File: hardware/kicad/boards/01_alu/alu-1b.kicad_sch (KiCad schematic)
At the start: 4 parts, among them U301 74HC86, U302 74LS08

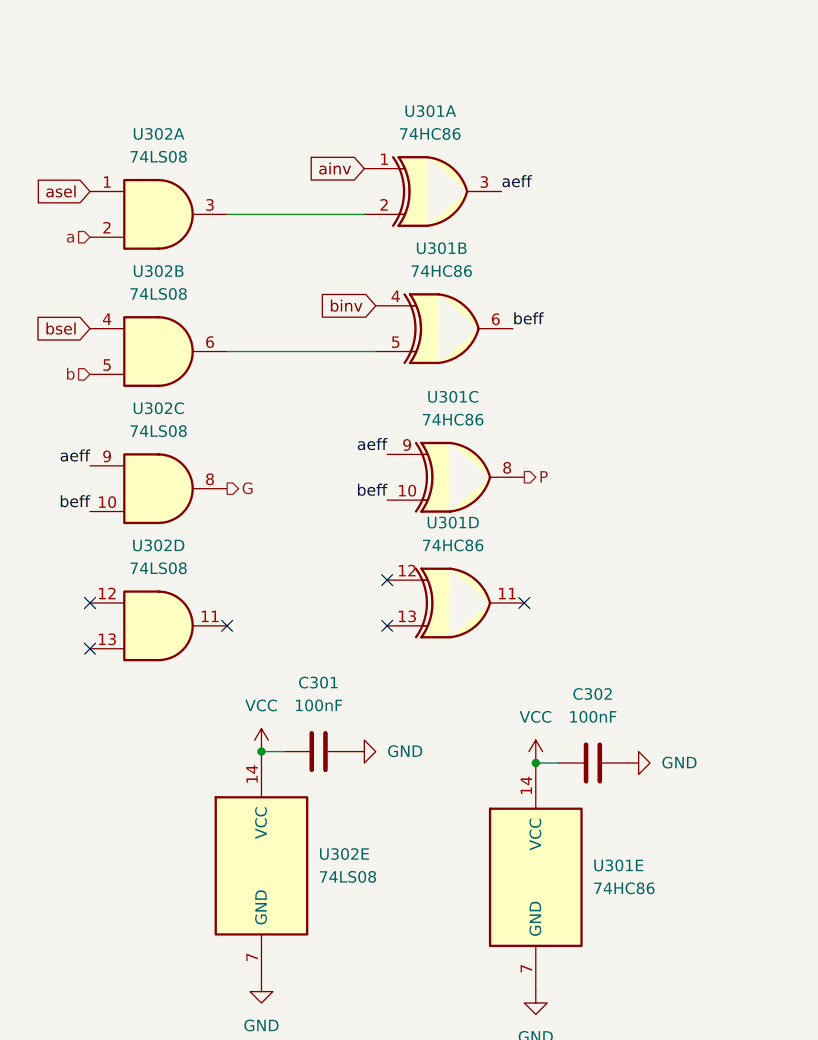
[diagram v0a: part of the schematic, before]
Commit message: arch: added LEDs, override switches; fixed errors and warnings to 0
ready for routing after logical coherence check
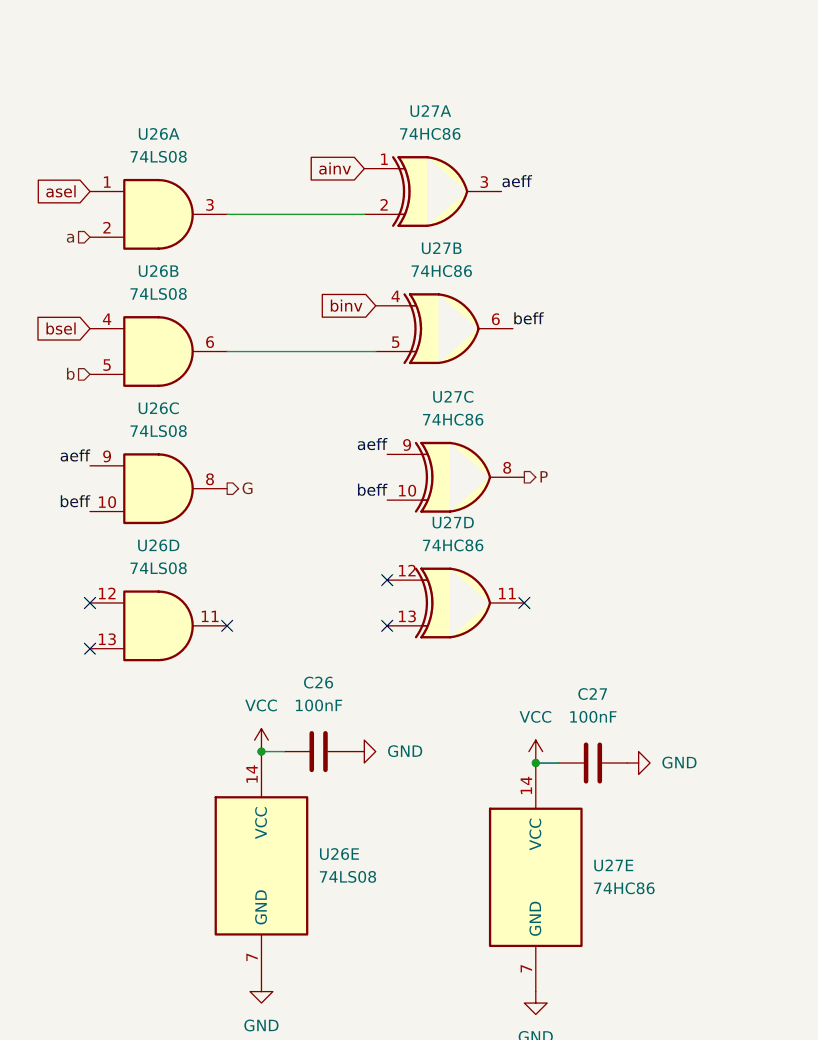
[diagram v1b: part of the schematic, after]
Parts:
- removed U302: 74LS08, Package_SO:SOIC-14_3.9x8.7mm_P1.27mm, symbol 74xx:74LS08
- added U26: 74LS08, Package_SO:SOIC-14_3.9x8.7mm_P1.27mm, symbol 74xx:74LS08
- renumbered C301 to C26, C302 to C27, U301 to U27
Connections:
- net G: now also U26.8
- net GND: now also U26.7 (GND)
- net VCC: now also U26.14 (VCC)
- net a: now also U26.2
- net aeff: now also U26.9
- net asel: now also U26.1
- net b: now also U26.5
- net beff: now also U26.10
- net bsel: now also U26.4
- net at U27.2: now also U26.3
- net at U27.5: now also U26.6

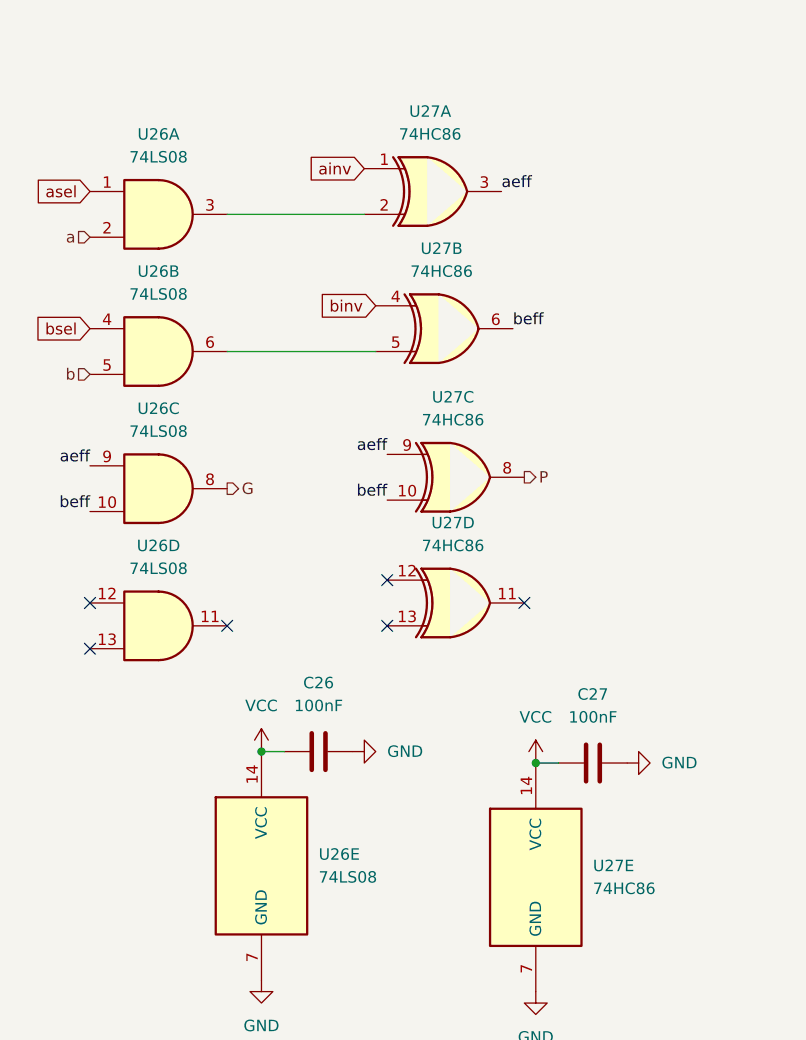
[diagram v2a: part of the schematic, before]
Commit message: design: designed and locked in pcb dimension and component placements
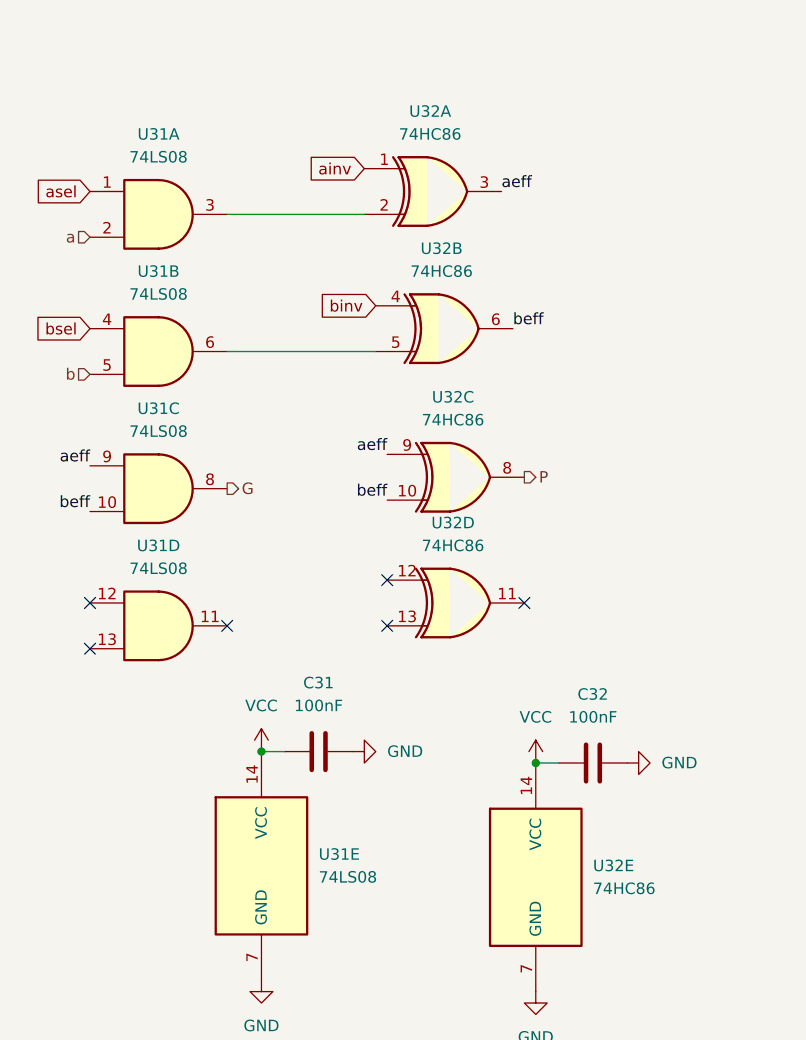
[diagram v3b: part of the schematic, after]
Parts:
- renumbered C26 to C31, C27 to C32, U26 to U31, U27 to U32

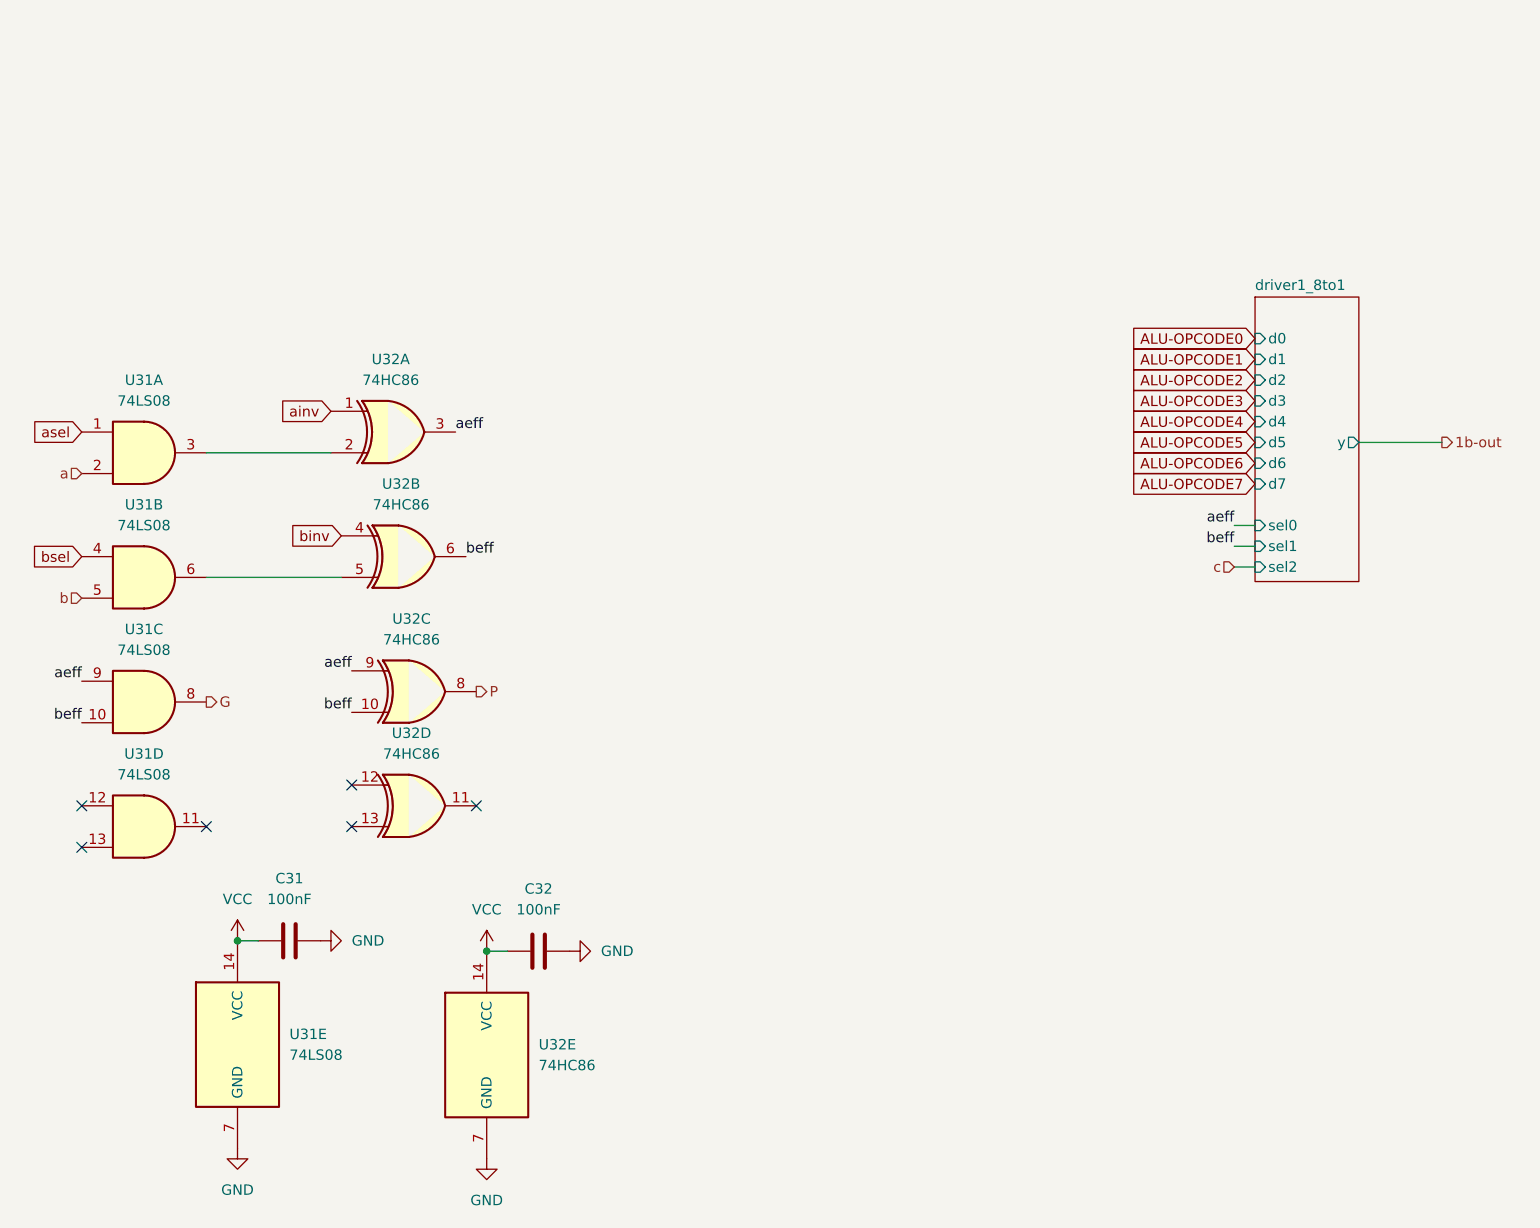
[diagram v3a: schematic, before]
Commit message: arch: replaced 3 footpring 125+138 with one strong 8to1 mux
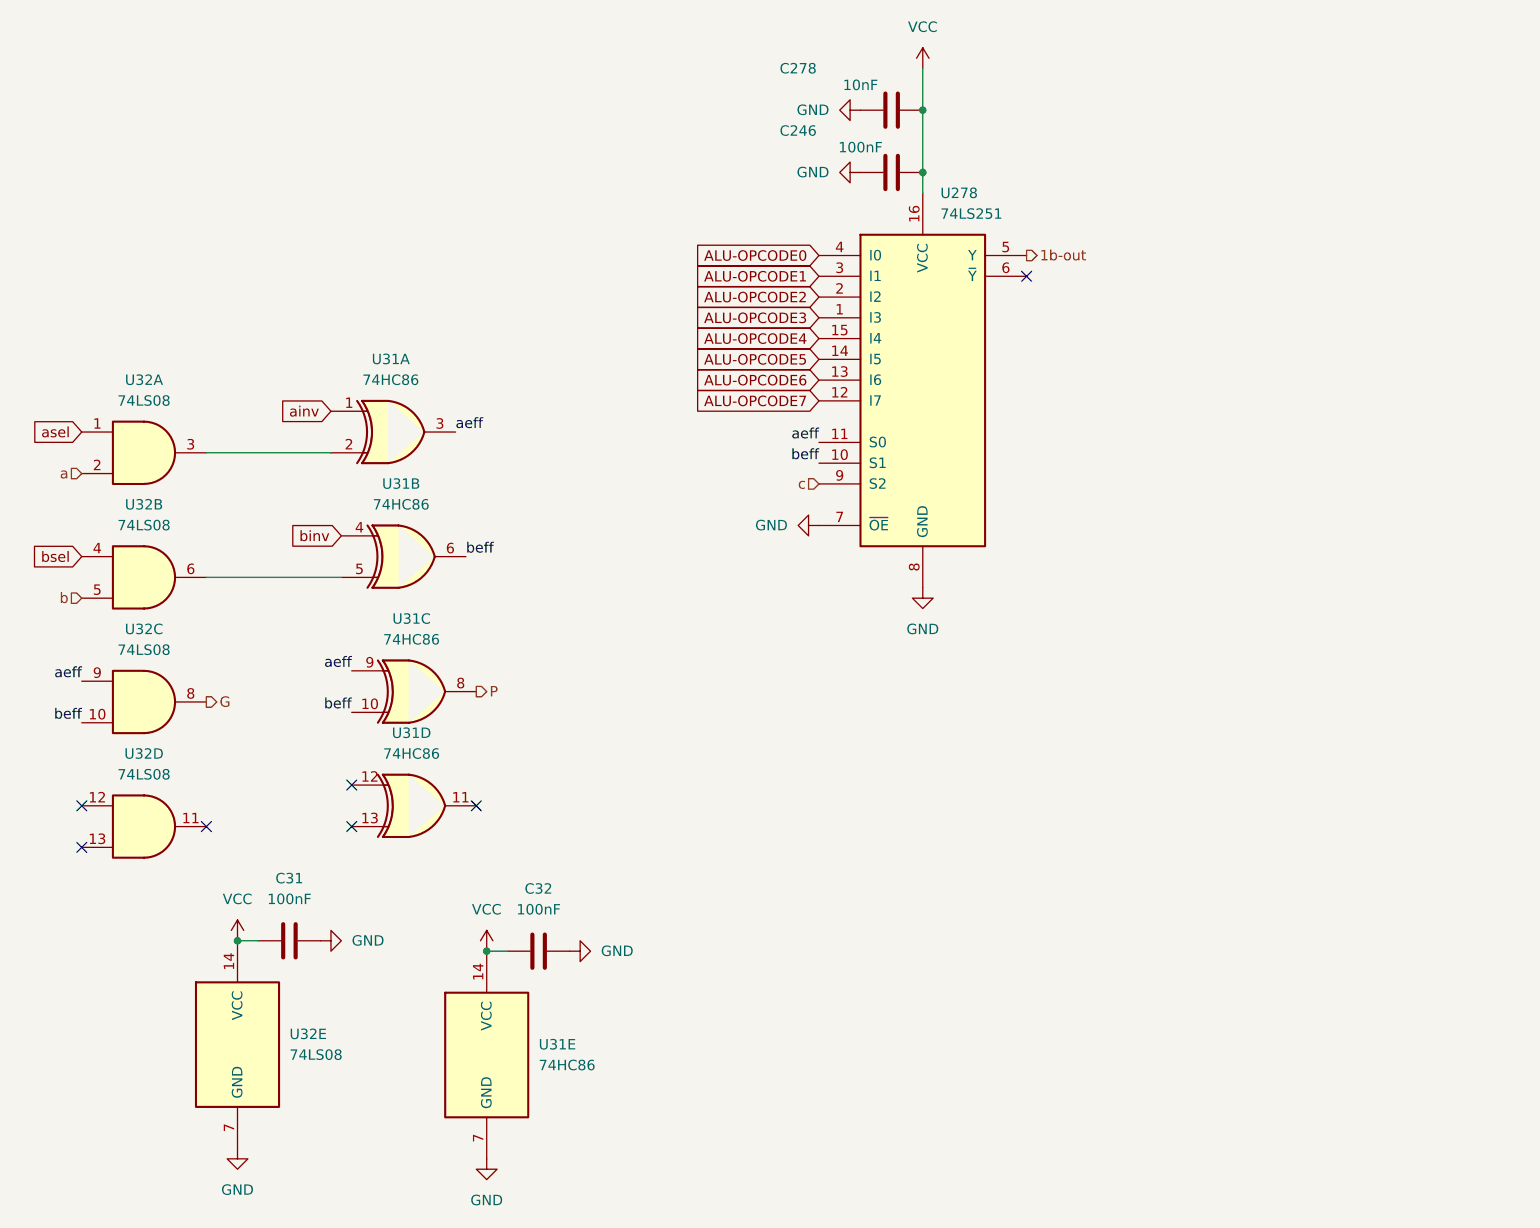
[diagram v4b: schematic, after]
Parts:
- added C246: 100nF, Capacitor_SMD:C_0603_1608Metric, symbol Device:C
- added C278: 10nF, Capacitor_SMD:C_0603_1608Metric, symbol Device:C
- added U278: 74LS251, symbol 74xx:74LS251
- C31, C32: footprint Capacitor_SMD:C_0805_2012Metric -> Capacitor_SMD:C_0603_1608Metric
- renumbered U32 to U31, U31 to U32
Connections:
- net 1b-out: now also U278.5 (Y)
- net ALU-OPCODE0: now also U278.4 (I0)
- net ALU-OPCODE1: now also U278.3 (I1)
- net ALU-OPCODE2: now also U278.2 (I2)
- net ALU-OPCODE3: now also U278.1 (I3)
- net ALU-OPCODE4: now also U278.15 (I4)
- net ALU-OPCODE5: now also U278.14 (I5)
- net ALU-OPCODE6: now also U278.13 (I6)
- net ALU-OPCODE7: now also U278.12 (I7)
- net GND: now also C246.1, C278.1, U278.7 (~{OE}), U278.8 (GND)
- net VCC: now also C246.2, C278.2, U278.16 (VCC)
- net aeff: now also U278.11 (S0)
- net beff: now also U278.10 (S1)
- net c: now also U278.9 (S2)
- no-connect marks 6 -> 7
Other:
- removed sheet driver1_8to1

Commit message: schematics: designed alu into 4b slices saving several chips and "de-bloating" board of several glue and drivers
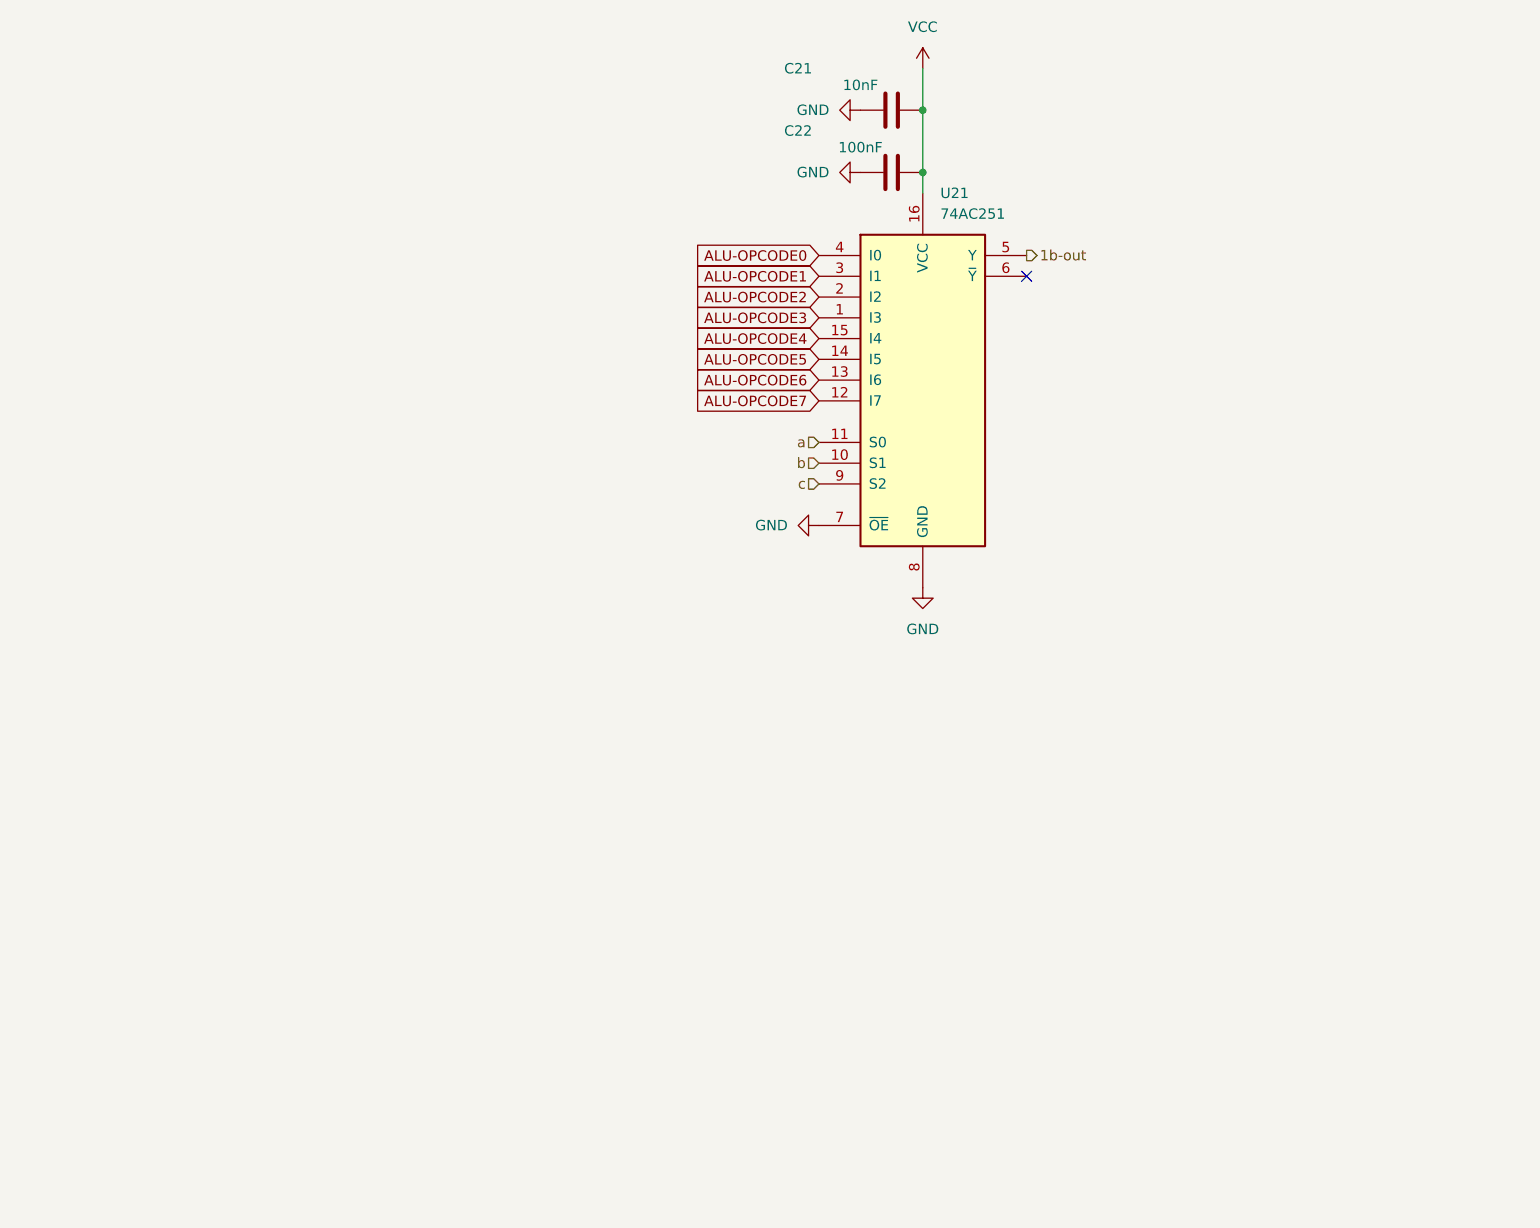
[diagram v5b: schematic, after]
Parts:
- removed C31, C32: 100nF, Capacitor_SMD:C_0603_1608Metric, symbol Device:C
- removed U31: 74HC86, Package_SO:SOIC-14_3.9x8.7mm_P1.27mm, symbol 74xx:74HC86
- removed U32: 74LS08, Package_SO:SOIC-14_3.9x8.7mm_P1.27mm, symbol 74xx:74LS08
- U21: renamed from U278; value 74LS251 -> 74AC251; footprint (none) -> Package_SO:SOIC-16_3.9x9.9mm_P1.27mm
- renumbered C278 to C21, C246 to C22
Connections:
- net aeff is gone; now on net a: U21.11 (S0)
- net beff is gone; now on net b: U21.10 (S1)
- no-connect marks 7 -> 1

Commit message: checkpoint: placed components for optimized routing on alu-32b board pcb
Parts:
- removed C21: 10nF, Capacitor_SMD:C_0603_1608Metric, symbol Device:C
